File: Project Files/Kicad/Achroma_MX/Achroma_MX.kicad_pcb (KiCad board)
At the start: 2 copper layers, 116.6 x 99.4 mm, 77 parts, among them SW1 RESET, SW2 SW_SPDT_312, U2 nice_nano

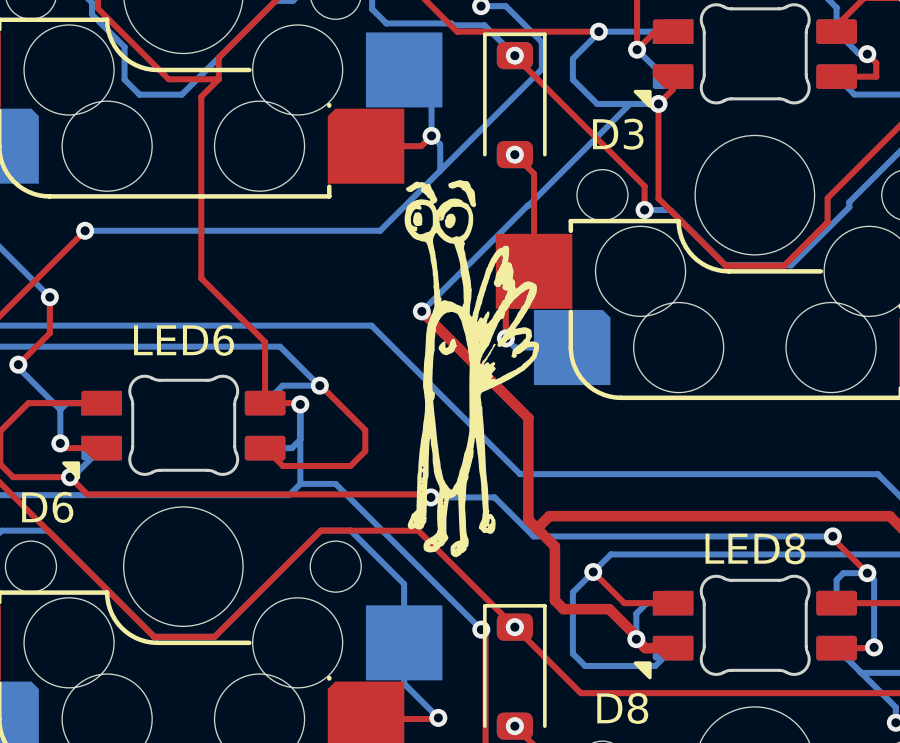
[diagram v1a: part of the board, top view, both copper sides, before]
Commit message: updated project files and imported Gerber
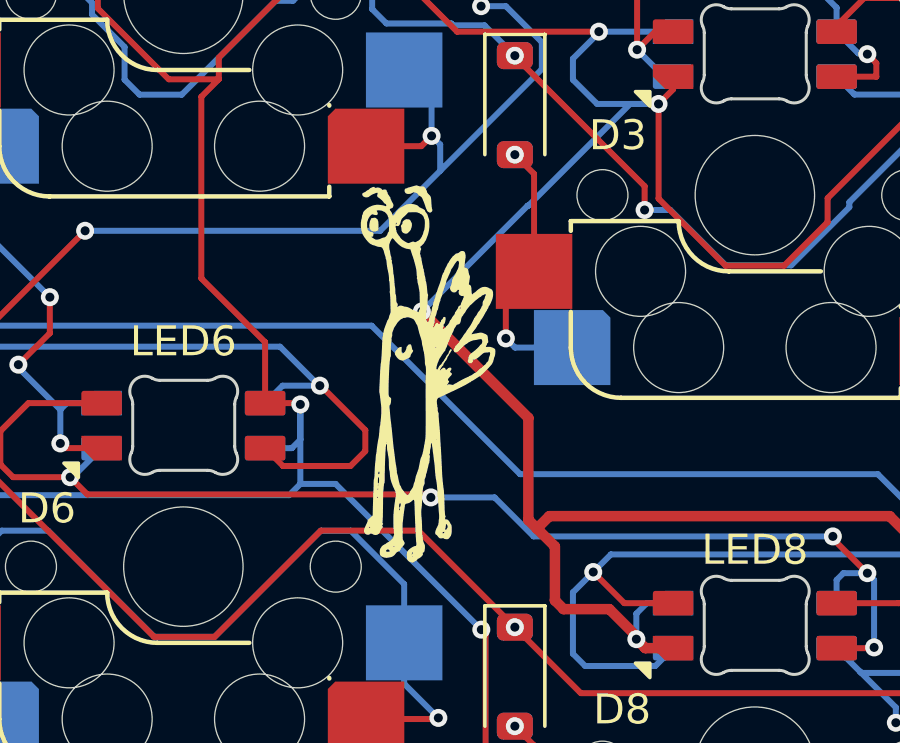
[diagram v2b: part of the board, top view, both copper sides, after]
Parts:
- moved G*** 1.47 mm to (82.3, 71.8)
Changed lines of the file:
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@@
 		(fp_line
 			(start -2.36 1)
-			(end 1.650002 1)
+			(end 1.650003 1)
 			(stroke
 				(width 0.12)
@@
 		(fp_line
 			(start 2.36 -1)
-			(end -1.650002 -1)
+			(end -1.650003 -1)
 			(stroke
 				(width 0.12)
@@
 		(fp_poly
 			(pts
-				(xy -3.5 1.25) (xy -3.5 1.73) (xy -3.98 1.250002) (xy -3.5 1.25)
+				(xy -3.5 1.25) (xy -3.5 1.73) (xy -3.98 1.250003) (xy -3.5 1.25)
 			)
 			(stroke
@@
 		(fp_poly
 			(pts
-				(xy -3.5 1.250001) (xy -3.5 1.730001) (xy -3.98 1.250003) (xy -3.5 1.250001)
+				(xy -3.5 1.250001) (xy -3.5 1.730001) (xy -3.98 1.250004) (xy -3.5 1.250001)
 			)
 			(stroke
@@
 		(fp_line
 			(start -1.687526 -0.713774)
-			(end -1.687526 0.691908)
+			(end -1.687526 0.691907)
 			(stroke
 				(width 0.1)
@@
 		)
 		(fp_arc
-			(start -1.687526 0.691908)
+			(start -1.687526 0.691907)
 			(mid -1.700054 0.803136)
 			(end -1.737011 0.908788)
@@
 	(footprint "LOGO"
 		(layer "F.Cu")
-		(at 83.76 71.62)
+		(at 82.3 71.8)
 		(property "Reference" "G***"
 			(at 0 0 0)
